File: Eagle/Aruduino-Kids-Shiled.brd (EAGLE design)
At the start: 86.4 x 52.8 mm, 16 parts

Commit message: Second
few changes
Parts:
- added U$3: SIPS-7, Aruduino-Kids-Shiled:SIPC-7
- U$6: value C-03784 -> SIPS-2; device Aruduino-Kids-Shiled:SIPC-6 -> Aruduino-Kids-Shiled:SIPC-2
- moved U$6 46.0 mm to (42.3, 52.6), turned to 90 degrees
- moved 0-50C 5.84 mm to (30.5, 14.7)
- moved TACTSW2 0.76 mm to (66.5, 49.0)
- turned VR.1 to 0 degrees
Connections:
- new net N$25: U$1.P$13, U$3.P$7
- new net N$26: U$1.P$16, U$6.P$1
- new net N$27: U$1.P$15, U$6.P$2
- net N$10: now also U$3.P$1; no longer U$6.P$1
- net N$12: now also U$3.P$4; no longer U$6.P$6
- net N$14: now also U$3.P$2; no longer U$6.P$2
- net N$15: now also U$3.P$3; no longer U$6.P$3
- net N$16: now also U$1.P$5, U$3.P$5; no longer U$1.P$4, U$6.P$4
- net N$17: now also U$1.P$4, U$3.P$6; no longer U$1.P$5, U$6.P$5
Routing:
- net N$25: track 0.00 -> 43.0 mm
- net N$12: track 53.9 -> 27.3 mm
- net N$26: track 0.00 -> 13.8 mm
- net N$27: track 0.00 -> 12.6 mm
- net N$4: track 23.2 -> 31.6 mm
- net N$16: track 17.9 -> 24.8 mm, vias 0 -> 2
- net N$7: track 43.6 -> 40.0 mm
- net N$17: track 21.6 -> 24.8 mm
- net N$6: track 115.7 -> 113.2 mm
- net N$14: track 10.6 -> 8.64 mm
- net N$15: track 23.3 -> 22.2 mm, vias 1 -> 0
- net N$10: track 5.57 -> 4.46 mm
- net N$11: track 65.4 -> 66.1 mm
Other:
- board text added: "C1-0.1uF"
- board text added: "LED1"
- board text added: "LED2"
- board text added: "R1-100KΩ"
- board text added: "RX"
- board text added: "Serial"
- board text added: "TACT-SW-1"
- board text added: "TACT-SW-2"
- board text added: "TP1-OUT (2A)"
- board text added: "TX"
- board text added: "TogSW1"
- board text added: "dp13-(AnalogIn)"
- board text added: "dp27-(SCl-I2C)"
- board text added: "dp5-(sda-I2C)"
- board text removed: "dp27-(scl_I2C)"
- board text removed: "dp5-(sda_I2C)"

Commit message: Semi_Final
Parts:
- moved TB2 27.3 mm to (81.3, 23.8), turned to 0 degrees
- moved TB1 27.2 mm to (81.3, 34.5), turned to 0 degrees
- moved U$4 11.3 mm to (60.3, 34.5), turned to 90 degrees
- moved LED1 10.4 mm to (45.3, 29.7)
- moved LED2 10.4 mm to (45.3, 36.6)
- moved U$2 10.2 mm to (41.8, 10.4)
- moved R1 10.2 mm to (41.8, 20.9)
- moved C1 10.2 mm to (41.9, 16.7)
- moved VR.1 7.16 mm to (5.46, 7.82)
- moved U$5 6.85 mm to (60.3, 23.8), turned to 90 degrees
- moved U$3 5.57 mm to (2.10, 24.4)
- moved U$6 4.70 mm to (43.4, 48.0)
- moved T-SW1 4.30 mm to (79.2, 44.7)
- moved TACTSW1 4.30 mm to (53.8, 44.7)
- moved TACTSW2 4.30 mm to (66.5, 44.7)
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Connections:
- net N$1 renamed GND
- net N$19 renamed P18
- net N$2 renamed P14
- net N$20 renamed P24
- net N$3 renamed P28
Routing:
- net P24: track 73.3 -> 84.8 mm, vias 1 -> 0
- net GND: track 168.8 -> 180.0 mm
- net N$8: track 42.5 -> 53.6 mm
- net P18: track 70.7 -> 61.2 mm, vias 1 -> 0
- net P14: track 6.98 -> 16.4 mm
- net P28: track 44.5 -> 51.5 mm
- net N$25: track 43.0 -> 49.8 mm
- net N$6: track 113.2 -> 107.0 mm
- net N$5: track 47.4 -> 50.8 mm
- net N$27: track 12.6 -> 14.9 mm
- net N$99: track 0.00 -> 2.31 mm
- net N$7: track 40.0 -> 42.2 mm, vias 2 -> 0
- net N$14: track 8.64 -> 10.5 mm
- net N$9: track 40.9 -> 39.6 mm
- net N$10: track 4.46 -> 5.73 mm
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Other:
- board size 86.4 x 52.8 mm -> 86 x 53 mm
- board text added: "TP1 ー (2A)＋"
- board text added: "TP2 ー(2A)＋"
- board text added: "Tr1"
- board text added: "Tr2"
- board text added: "dp27-(scl-I2C)"
- board text removed: "C1-0.1uF"
- board text removed: "LED1"
- board text removed: "LED2"
- board text removed: "R1-100KΩ"
- board text removed: "TACT-SW-1"
- board text removed: "TACT-SW-2"
- board text removed: "TP1-OUT (2A)"
- board text removed: "TogSW1"
- board text removed: "dp27-(SCl-I2C)"

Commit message: Practice-Final
Test-Build
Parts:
- added R2: 1K, Aruduino-Kids-Shiled:R12MM
- added U$10, U$9: SIPS-2, Aruduino-Kids-Shiled:SIPC-2
- added U$7: (no value), frames:A4L-LOC
- R1: value 100K -> 10K
- TACTSW1, TACTSW2: value SW -> (none)
- moved LED2 8.26 mm to (45.3, 28.4), turned to 0 degrees
- moved LED1 6.86 mm to (45.3, 36.5), turned to 0 degrees
- moved VR.1 2.00 mm to (5.46, 5.82)
- moved TACTSW2 1.12 mm to (67.5, 45.4), turned to 180 degrees
- moved U$3 1.10 mm to (2.16, 23.3)
- moved TACTSW1 0.95 mm to (54.5, 45.4), turned to 180 degrees
- moved R1 0.76 mm to (41.8, 21.7), turned to 180 degrees
- moved T-SW1 0.70 mm to (79.2, 45.4)
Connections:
- removed net N$7: U$1.P$8, VR.1.P$1
- new net N$33: 0-50C.2, R2.2, U$1.P$10
- net GND: now also LED1.K, LED2.K, TACTSW1.2, TACTSW2.2, U$10.P$2, U$9.P$2; no longer LED1.A, LED2.A, TACTSW1.3, TACTSW2.3
- net N$11: now also TACTSW2.3; no longer TACTSW2.2
- net N$4: now also R2.1, U$1.P$7, U$2.P$2, VR.1.P$3; no longer 0-50C.2, U$1.P$10
- net N$5: now also R1.1; no longer R1.2
- net N$6: now also R1.2, U$1.P$8, VR.1.P$1; no longer R1.1, U$1.P$7, U$2.P$2, VR.1.P$3
- net N$8: now also U$3.P$8
- net N$9: now also TACTSW1.3; no longer TACTSW1.2
- net P14: now also LED1.A; no longer LED1.K
- net P18: now also U$10.P$1
- net P24: now also U$9.P$1
- net P28: now also LED2.A; no longer LED2.K
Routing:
- net N$169: track 0.00 -> 191.4 mm, vias 0 -> 19
- net N$148: track 0.00 -> 191.4 mm, vias 0 -> 19
- net N$4: track 30.9 -> 109.6 mm, vias 0 -> 1
- net P18: track 61.2 -> 101.3 mm, vias 0 -> 2
- net N$133: track 0.00 -> 39.6 mm, vias 0 -> 9
- net N$101: track 0.00 -> 39.6 mm, vias 0 -> 9
- net N$33: track 0.00 -> 31.2 mm, vias 1 -> 0
- net N$7: track 42.2 -> 11.1 mm
- net N$116: track 0.00 -> 29.5 mm
- net N$30: track 0.00 -> 29.5 mm, vias 1 -> 0
- net N$168: track 0.00 -> 29.2 mm
- net N$147: track 0.00 -> 29.2 mm
- net N$117: track 0.00 -> 27.7 mm
- net N$6: track 107.0 -> 83.2 mm, vias 0 -> 2
- net N$134: track 0.00 -> 20.6 mm
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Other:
- board text added: "GND"
- board text added: "NTC"
- board text added: "PHOTO-IC"
- board text added: "TP1"
- board text added: "TP1 ー(2A)＋"
- board text added: "TP2"
- board text added: "TP2 ー (2A)＋"
- board text added: "TP3"
- board text added: "TP4"
- board text added: "dp18"
- board text added: "dp24"
- board text added: "dp8-(AnalogGND)"
- board text added: "mbed 1114FN28"
- board text removed: "TP1 ー (2A)＋"
- board text removed: "TP2 ー(2A)＋"

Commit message: Final-P-ban
1st time
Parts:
- R2: value 1K -> 7.5K
- moved U$6 0.23 mm to (43.4, 47.8)
- moved U$2 0.08 mm to (41.8, 10.5)
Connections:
- net GND renamed N$126
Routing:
- net N$6: track 83.2 -> 126.1 mm
- net N$4: track 109.6 -> 149.9 mm
- net N$9: track 30.3 -> 35.7 mm
- net N$11: track 60.2 -> 63.3 mm
- net N$115: track 3.05 -> 0.00 mm
- net P28: track 57.6 -> 59.8 mm
- net N$119: track 0.00 -> 2.12 mm
- net N$127: track 0.00 -> 1.80 mm
- net N$27: track 14.7 -> 13.1 mm
- net N$35: track 4.62 -> 6.19 mm
- net N$125: track 0.00 -> 1.46 mm
- net N$121: track 0.00 -> 1.44 mm
- net N$120: track 0.00 -> 0.94 mm
- net N$128: track 0.00 -> 0.84 mm
- net N$33: track 31.2 -> 32.0 mm
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
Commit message: Test-Sample-Build
Jet-PCB
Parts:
- LED1: value 5V-12mA-Include-R -> I-06245-R
- LED2: value 5V-12mA-Include-R -> I-06245-G
- T-SW1: value SW -> P-00300
- TACTSW1: value (none) -> P-03646-B
- TACTSW2: value (none) -> P-03646-R
- TB1, TB2: value 2A -> P-01306
- moved VR.1 6.17 mm to (11.6, 5.81)
- moved T-SW1 1.78 mm to (77.5, 45.4)
- moved TACTSW2 1.42 mm to (66.0, 45.4)
- moved C1 0.86 mm to (41.9, 15.8)
- moved R1 0.66 mm to (41.8, 21.0)
- moved U$2 0.31 mm to (41.9, 10.2)
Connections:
- net N$126 renamed GND
- net N$4 renamed 3.3V
- removed net N$6: 0-50C.1, C1.1, R1.2, U$1.P$8, VR.1.P$1
- new net A-GND: 0-50C.1, C1.1, R1.2, U$1.P$8, U$3.P$8, VR.1.P$1
- net N$8: no longer U$3.P$8
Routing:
- net A-GND: track 0.00 -> 139.6 mm, vias 0 -> 2
- net N$6: track 126.1 -> 3.97 mm, vias 2 -> 0
- net 3.3V: track 149.9 -> 98.3 mm
- net GND: track 198.9 -> 217.8 mm
- net N$8: track 64.7 -> 48.8 mm
- net N$7: track 11.1 -> 0.00 mm
- net N$35: track 6.19 -> 0.99 mm
- net N$11: track 63.3 -> 59.3 mm
- net N$99: track 2.66 -> 0.00 mm
- net N$18: track 84.1 -> 82.4 mm
- net N$13: track 75.0 -> 73.3 mm
- net N$125: track 1.46 -> 0.00 mm
- net N$128: track 0.84 -> 0.00 mm
- net N$34: track 0.75 -> 0.00 mm
- net N$4: track 0.00 -> 0.67 mm
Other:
- board text added: "P1 ー(2A)＋"
- board text added: "P2 ー (2A)＋"
- board text removed: "TP1 ー(2A)＋"
- board text removed: "TP2 ー (2A)＋"

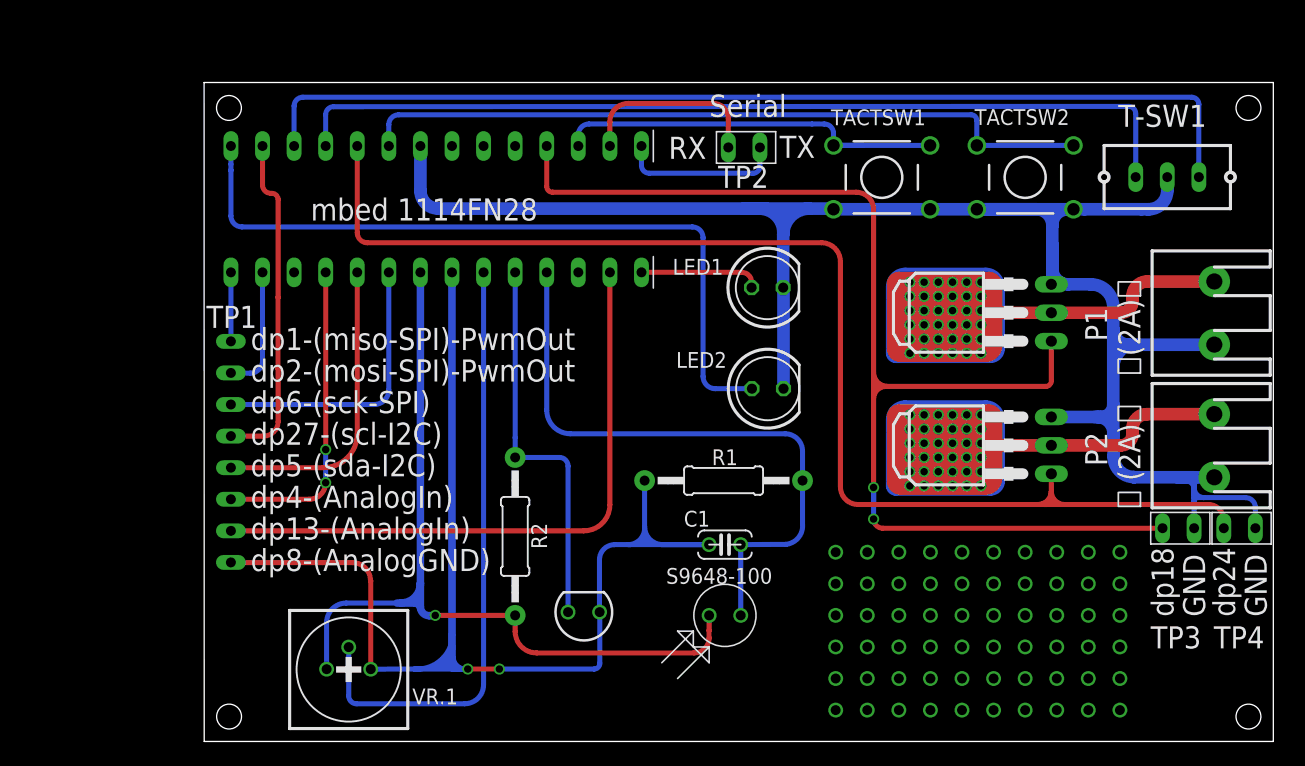
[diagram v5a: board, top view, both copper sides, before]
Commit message: Add dimensions
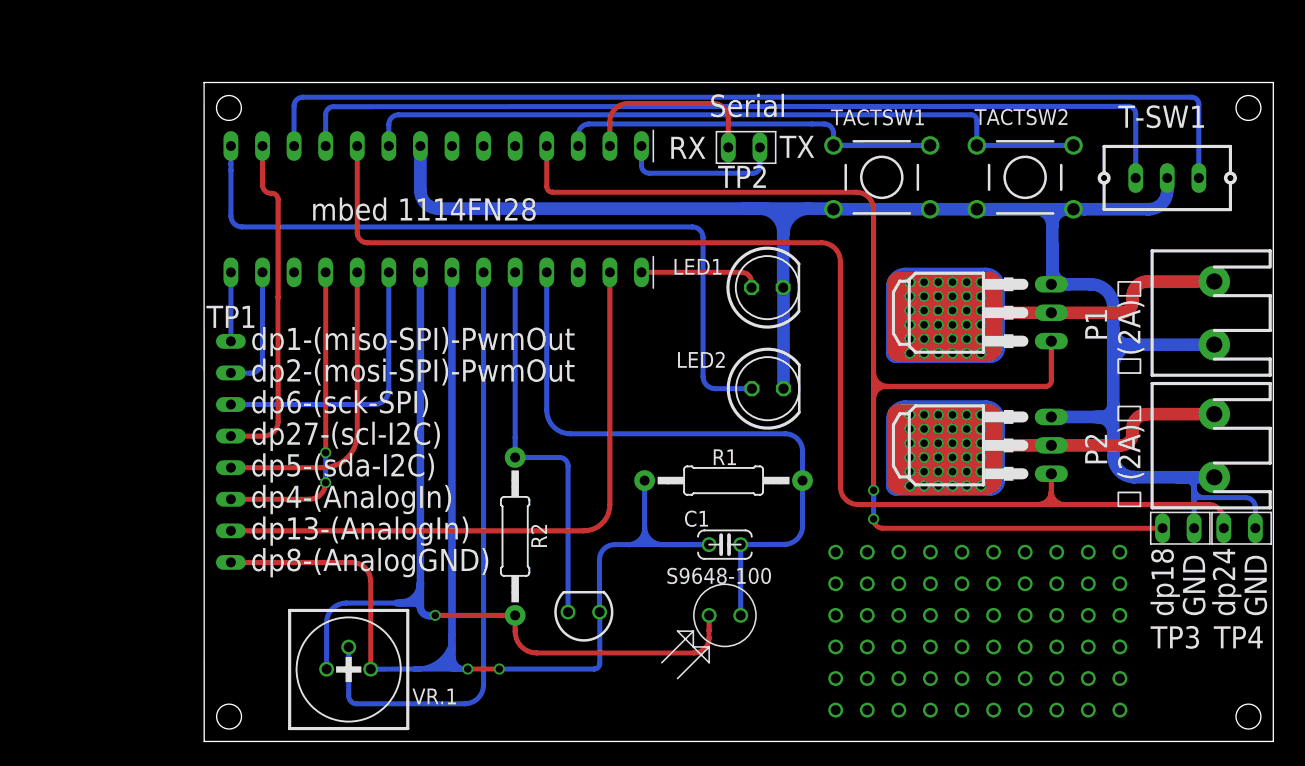
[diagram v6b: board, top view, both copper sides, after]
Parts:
- moved T-SW1 0.08 mm to (77.5, 45.3)
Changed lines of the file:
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@@
 <dimension x1="0" y1="53.018" x2="86.0044" y2="51.6636" x3="43.0022" y3="59.9186" textsize="1.778" layer="20" dtype="horizontal" visible="yes"/>
 <dimension x1="86" y1="53.018" x2="77.7494" y2="0" x3="102.3874" y3="26.509" textsize="1.778" layer="20" dtype="vertical" precision="1" visible="yes"/>
-<dimension x1="2.58005" y1="1.532615625" x2="1.43995" y2="2.507384375" x3="-1.193803125" y3="-1.727196875" textsize="1.778" layer="20" dtype="diameter" visible="yes"/>
+<dimension x1="3.01" y1="2.019228125" x2="1.01" y2="2.020771875" x3="2.006596875" y3="-2.3876" textsize="1.778" layer="44" dtype="diameter" visible="yes"/>
 </plain>
 <attributes>
@@
 </element>
 <element name="0-50C" library="Aruduino-Kids-Shiled" package="NTC" value="NTC-103-AT-2" x="30.5435" y="10.4218" smashed="yes" rot="R180"/>
-<element name="T-SW1" library="Aruduino-Kids-Shiled" package="TOGLE-SW" value="P-00300" x="77.47" y="45.4103" smashed="yes" rot="R90">
-<attribute name="NAME" x="73.533" y="49.4538" size="1.778" layer="25" ratio="10" rot="R180" align="top-right"/>
+<element name="T-SW1" library="Aruduino-Kids-Shiled" package="TOGLE-SW" value="P-00300" x="77.47" y="45.3341" smashed="yes" rot="R90">
+<attribute name="NAME" x="73.533" y="49.3776" size="1.778" layer="25" ratio="10" rot="R180" align="top-right"/>
 </element>
 <element name="TB1" library="Aruduino-Kids-Shiled" package="TB" value="P-01306" x="81.2526" y="34.4746"/>
@@
 <wire x1="7.945521875" y1="51.834" x2="79.4385" y2="51.834" width="0.4064" layer="16"/>
 <wire x1="79.4385" y1="51.834" x2="80.01" y2="51.2625" width="0.4064" layer="16" curve="-90"/>
-<wire x1="80.01" y1="51.2625" x2="80.01" y2="45.4103" width="0.4064" layer="16"/>
+<wire x1="80.01" y1="51.2625" x2="80.01" y2="45.3341" width="0.4064" layer="16"/>
 </signal>
 <signal name="N$13">
@@
 <wire x1="10.414" y1="51.072" x2="74.3585" y2="51.0974" width="0.4064" layer="16"/>
 <wire x1="74.3585" y1="51.0974" x2="74.93" y2="50.5259" width="0.4064" layer="16" curve="-90"/>
-<wire x1="74.93" y1="50.5259" x2="74.93" y2="45.4103" width="0.4064" layer="16"/>
+<wire x1="74.93" y1="50.5259" x2="74.93" y2="45.3341" width="0.4064" layer="16"/>
 </signal>
 <signal name="N$14">
@@
 <contactref element="U$1" pad="P$4"/>
 <contactref element="U$3" pad="P$6"/>
-<wire x1="9.779" y1="37.7498" x2="9.779" y2="23.495" width="0.4064" layer="1"/>
-<via x="9.779" y="23.495" extent="1-16" drill="0.6"/>
-<wire x1="9.779" y1="23.495" x2="9.779" y2="20.828" width="0.4064" layer="16"/>
+<wire x1="9.779" y1="37.7498" x2="9.779" y2="23.241" width="0.4064" layer="1"/>
+<via x="9.779" y="23.241" extent="1-16" drill="0.6"/>
+<wire x1="9.779" y1="23.241" x2="9.779" y2="20.828" width="0.4064" layer="16"/>
 <via x="9.779" y="20.828" extent="1-16" drill="0.6"/>
 <wire x1="9.779" y1="20.828" x2="8.449021875" y2="19.498021875" width="0.4064" layer="1" curve="-90"/>
@@
 <wire x1="67.691" y1="28.575" x2="68.1462" y2="29.0302" width="0.4064" layer="1" curve="90"/>
 <wire x1="68.1462" y1="29.0302" x2="68.1462" y2="32.214" width="0.4064" layer="1"/>
-<wire x1="53.848" y1="19.177" x2="53.848" y2="20.447" width="0.4064" layer="16"/>
-<via x="53.848" y="20.447" extent="1-16" drill="0.6"/>
+<wire x1="53.848" y1="19.177" x2="53.848" y2="20.2184" width="0.4064" layer="16"/>
+<via x="53.848" y="20.2184" extent="1-16" drill="0.6"/>
 <wire x1="53.848" y1="28.067" x2="53.848" y2="29.718" width="0.4064" layer="1"/>
 <wire x1="54.356" y1="28.575" x2="54.864" y2="28.575" width="0.4064" layer="1"/>
@@
 <wire x1="54.356" y1="28.575" x2="53.848" y2="28.067" width="0.4064" layer="1" curve="90"/>
 <wire x1="53.975" y1="28.575" x2="54.356" y2="28.575" width="0.4064" layer="1"/>
-<wire x1="53.848" y1="20.447" x2="53.848" y2="27.432" width="0.4064" layer="1"/>
+<wire x1="53.848" y1="20.2184" x2="53.848" y2="27.559" width="0.4064" layer="1"/>
 <contactref element="U$10" pad="P$1"/>
 <wire x1="53.848" y1="27.559" x2="53.848" y2="28.067" width="0.4064" layer="1"/>
@@
 <wire x1="54.5846" y1="17.1704" x2="53.848" y2="17.907" width="0.4064" layer="1" curve="-90"/>
 <via x="53.848" y="17.907" extent="1-16" drill="0.6"/>
-<wire x1="53.848" y1="17.907" x2="53.848" y2="20.447" width="0.4064" layer="16"/>
-<wire x1="53.848" y1="27.432" x2="53.848" y2="27.559" width="0.4064" layer="1"/>
+<wire x1="53.848" y1="17.907" x2="53.848" y2="20.2184" width="0.4064" layer="16"/>
 <wire x1="53.848" y1="27.559" x2="54.864" y2="28.575" width="0.4064" layer="1" curve="-90"/>
 </signal>
@@
 <wire x1="68.2244" y1="36.8642" x2="68.1462" y2="36.786" width="1.016" layer="16" curve="-90"/>
 <wire x1="75.9206" y1="42.8244" x2="75.9185" y2="42.8223" width="1.016" layer="16" curve="-90"/>
-<wire x1="75.9185" y1="42.8223" x2="75.3872" y2="42.8223" width="1.016" layer="16"/>
-<wire x1="75.3872" y1="42.8223" x2="70.8152" y2="42.8223" width="1.016" layer="16"/>
+<wire x1="75.9185" y1="42.8223" x2="70.8152" y2="42.8223" width="1.016" layer="16"/>
 <wire x1="70.8152" y1="42.8223" x2="69.925" y2="42.8223" width="1.016" layer="16"/>
 <wire x1="69.925" y1="42.8223" x2="69.4669" y2="42.8223" width="1.016" layer="16"/>
@@
 <wire x1="70.8152" y1="42.8223" x2="70.7877" y2="42.8498" width="0" layer="16" curve="90"/>
 <wire x1="70.7877" y1="42.8498" x2="70.0532" y2="42.8498" width="0" layer="16"/>
-<wire x1="77.47" y1="45.4103" x2="77.47" y2="44.323" width="1.016" layer="16"/>
+<wire x1="77.47" y1="45.3341" x2="77.47" y2="44.323" width="1.016" layer="16"/>
 <wire x1="77.47" y1="44.323" x2="75.9693" y2="42.8223" width="1.016" layer="16" curve="-90"/>
 <wire x1="75.9693" y1="42.8223" x2="75.9185" y2="42.8223" width="1.016" layer="16"/>
